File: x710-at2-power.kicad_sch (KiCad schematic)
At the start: 6 parts, among them U1 EZX710AT2_S_LMR5

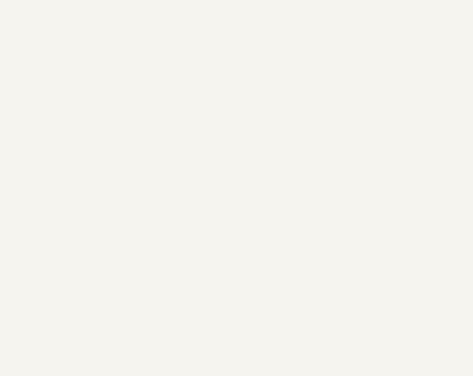
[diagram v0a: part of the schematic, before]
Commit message: [#80813] Add RJ45 connectors, add SMBus, FLASH SPI and misc
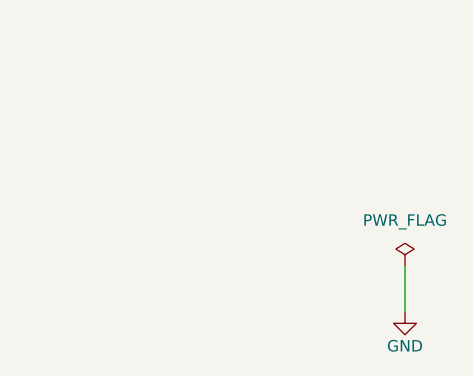
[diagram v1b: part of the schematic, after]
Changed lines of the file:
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@@
+	(wire
+		(pts
+			(xy 331.47 175.26) (xy 331.47 180.34)
+		)
+		(stroke
+			(width 0)
+			(type default)
+		)
+	)
 	(wire
 		(pts
@@
 					(unit 1)
 				)
+			)
+		)
+	)
+	(symbol
+		(lib_id "antmicropower:PWR_FLAG")
+		(at 331.47 175.26 0)
+		(unit 1)
+		(exclude_from_sim no)
+		(in_bom yes)
+		(on_board yes)
+		(dnp no)
+		(fields_autoplaced yes)
+		(property "Reference" "#FLG01"
+			(at 331.47 173.355 0)
+			(effects
+				(font
+					(size 1.27 1.27)
+				)
+				(hide yes)
+			)
+		)
+		(property "Value" "PWR_FLAG"
+			(at 331.47 170.18 0)
+			(effects
+				(font
+					(size 1.27 1.27)
+				)
+			)
+		)
+		(property "Footprint" ""
+			(at 331.47 175.26 0)
+			(effects
+				(font
+					(size 1.27 1.27)
+				)
+				(hide yes)
+			)
+		)
+		(property "Datasheet" ""
+			(at 331.47 175.26 0)
+			(effects
+				(font
+					(size 1.27 1.27)
+				)
+				(hide yes)
+			)
+		)
+		(property "Description" ""
+			(at 331.47 175.26 0)
+			(effects
+				(font
+					(size 1.27 1.27)
+				)
+				(hide yes)
+			)
+		)
+		(pin "1"
+		)
+		(instances
+			(project ""
+				(path "/04bda987-e5eb-48b4-9e90-d8211dc11b39/745fdd8b-25af-4553-a7ea-a0fa564ee0a7"
+					(reference "#FLG01")
+					(unit 1)
+				)
+			)
+		)
+	)
+	(symbol
+		(lib_id "antmicropower:GND")
+		(at 331.47 180.34 0)
+		(unit 1)
+		(exclude_from_sim no)
+		(in_bom yes)
+		(on_board yes)
+		(dnp no)
+		(property "Reference" "#PWR053"
+			(at 340.36 182.88 0)
+			(effects
+				(font
+					(size 1.27 1.27)
+					(thickness 0.15)
+				)
+				(justify left bottom)
+				(hide yes)
+			)
+		)
+		(property "Value" "GND"
+			(at 331.47 184.15 0)
+			(effects
+				(font
+					(size 1.27 1.27)
+					(thickness 0.15)
+				)
+			)
+		)
+		(property "Footprint" ""
+			(at 340.36 187.96 0)
+			(effects
+				(font
+					(size 1.27 1.27)
+					(thickness 0.15)
+				)
+				(justify left bottom)
+				(hide yes)
+			)
+		)
+		(property "Datasheet" ""
+			(at 340.36 193.04 0)
+			(effects
+				(font
+					(size 1.27 1.27)
+					(thickness 0.15)
+				)
+				(justify left bottom)
+				(hide yes)
+			)
+		)
+		(property "Description" ""
+			(at 331.47 180.34 0)
+			(effects
+				(font
+					(size 1.27 1.27)
+				)
+				(hide yes)
+			)
+		)
+		(property "Author" "Antmicro"
+			(at 340.36 187.96 0)
+			(effects
+				(font
+					(size 1.27 1.27)
+					(thickness 0.15)
+				)
+				(justify left bottom)
+				(hide yes)
+			)
+		)
+		(property "License" "Apache-2.0"
+			(at 340.36 190.5 0)
+			(effects
+				(font
+					(size 1.27 1.27)
+					(thickness 0.15)
+				)
+				(justify left bottom)
+				(hide yes)
+			)
+		)
+		(pin "1"
+		)
+		(instances
+			(project "10-gbe-expansion"
+				(path "/04bda987-e5eb-48b4-9e90-d8211dc11b39/745fdd8b-25af-4553-a7ea-a0fa564ee0a7"
+					(reference "#PWR053")
+					(unit 1)
+				)

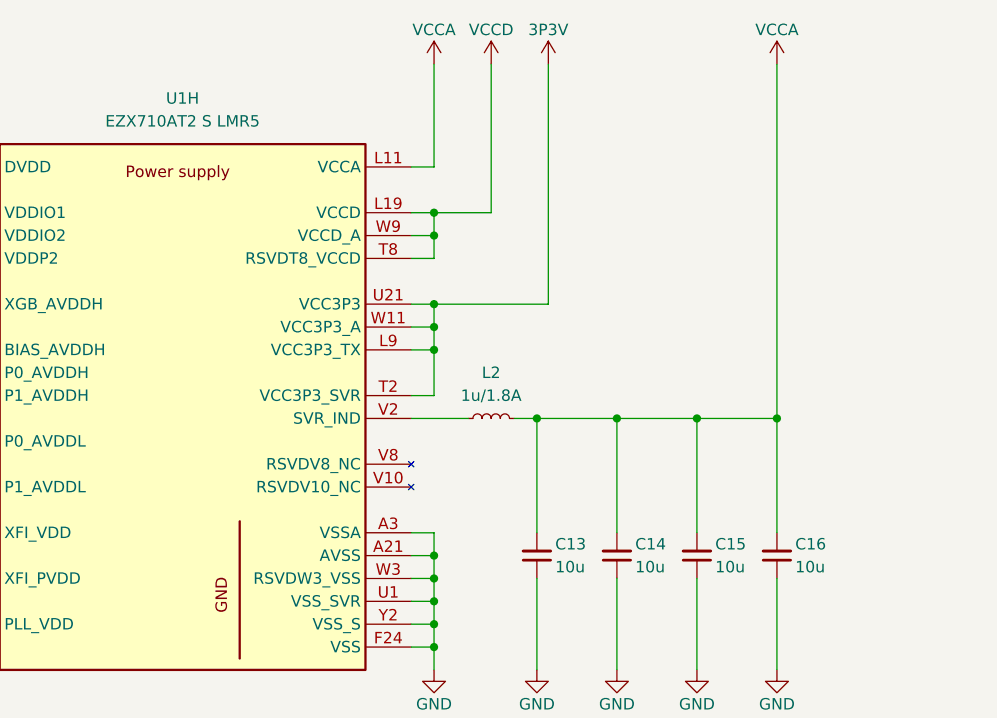
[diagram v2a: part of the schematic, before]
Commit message: [#80813] Change RJ45 connectors, reannotate schematics
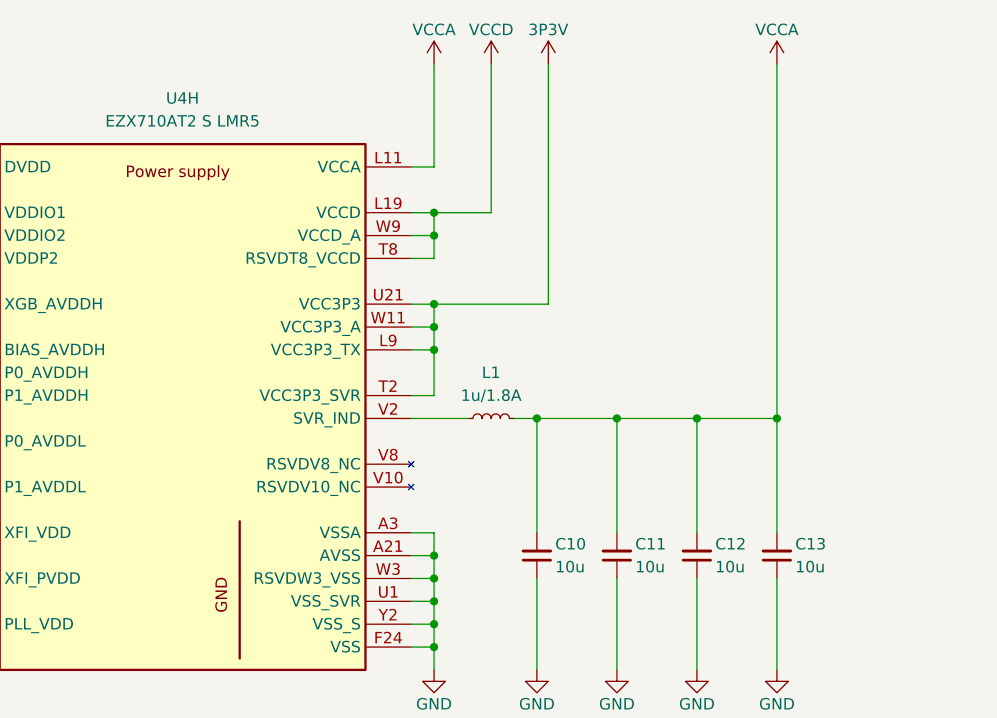
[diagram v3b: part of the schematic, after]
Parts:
- renumbered C13 to C10, C14 to C11, C15 to C12, C16 to C13, L2 to L1, U1 to U4
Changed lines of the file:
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@@
 		(on_board yes)
 		(dnp no)
-		(property "Reference" "C13"
+		(property "Reference" "C10"
 			(at 253.492 166.37 90)
 			(effects
@@
 			(project "10-gbe-expansion"
 				(path "/04bda987-e5eb-48b4-9e90-d8211dc11b39/745fdd8b-25af-4553-a7ea-a0fa564ee0a7"
-					(reference "C13")
+					(reference "C10")
 					(unit 1)
 				)
@@
 		(on_board yes)
 		(dnp no)
-		(property "Reference" "C16"
+		(property "Reference" "C13"
 			(at 280.162 166.37 90)
 			(effects
@@
 			(project "10-gbe-expansion"
 				(path "/04bda987-e5eb-48b4-9e90-d8211dc11b39/745fdd8b-25af-4553-a7ea-a0fa564ee0a7"
-					(reference "C16")
+					(reference "C13")
 					(unit 1)
 				)
@@
 		(on_board yes)
 		(dnp no)
-		(property "Reference" "#PWR035"
+		(property "Reference" "#PWR039"
 			(at 278.13 116.84 0)
 			(effects
@@
 			(project "10-gbe-expansion"
 				(path "/04bda987-e5eb-48b4-9e90-d8211dc11b39/745fdd8b-25af-4553-a7ea-a0fa564ee0a7"
-					(reference "#PWR035")
+					(reference "#PWR039")
 					(unit 1)
 				)
@@
 		(on_board yes)
 		(dnp no)
-		(property "Reference" "#PWR031"
+		(property "Reference" "#PWR041"
 			(at 260.35 182.88 0)
 			(effects
@@
 			(project "10-gbe-expansion"
 				(path "/04bda987-e5eb-48b4-9e90-d8211dc11b39/745fdd8b-25af-4553-a7ea-a0fa564ee0a7"
-					(reference "#PWR031")
+					(reference "#PWR041")
 					(unit 1)
 				)
@@
 		(on_board yes)
 		(dnp no)
-		(property "Reference" "#PWR033"
+		(property "Reference" "#PWR042"
 			(at 269.24 182.88 0)
 			(effects
@@
 			(project "10-gbe-expansion"
 				(path "/04bda987-e5eb-48b4-9e90-d8211dc11b39/745fdd8b-25af-4553-a7ea-a0fa564ee0a7"
-					(reference "#PWR033")
+					(reference "#PWR042")
 					(unit 1)
 				)
@@
 		(on_board yes)
 		(dnp no)
-		(property "Reference" "#PWR053"
+		(property "Reference" "#PWR045"
 			(at 340.36 182.88 0)
 			(effects
@@
 			(project "10-gbe-expansion"
 				(path "/04bda987-e5eb-48b4-9e90-d8211dc11b39/745fdd8b-25af-4553-a7ea-a0fa564ee0a7"
-					(reference "#PWR053")
+					(reference "#PWR045")
 					(unit 1)
 				)
@@
 		(on_board yes)
 		(dnp no)
-		(property "Reference" "C15"
+		(property "Reference" "C12"
 			(at 271.272 166.37 90)
 			(effects
@@
 			(project "10-gbe-expansion"
 				(path "/04bda987-e5eb-48b4-9e90-d8211dc11b39/745fdd8b-25af-4553-a7ea-a0fa564ee0a7"
-					(reference "C15")
+					(reference "C12")
 					(unit 1)
 				)
@@
 		(on_board yes)
 		(dnp no)
-		(property "Reference" "#PWR025"
+		(property "Reference" "#PWR033"
 			(at 166.37 116.84 0)
 			(effects
@@
 			(project "10-gbe-expansion"
 				(path "/04bda987-e5eb-48b4-9e90-d8211dc11b39/745fdd8b-25af-4553-a7ea-a0fa564ee0a7"
-					(reference "#PWR025")
+					(reference "#PWR033")
 					(unit 1)
 				)
@@
 		(on_board yes)
 		(dnp no)
-		(property "Reference" "#PWR027"
+		(property "Reference" "#PWR035"
 			(at 184.15 116.84 0)
 			(effects
@@
 			(project "10-gbe-expansion"
 				(path "/04bda987-e5eb-48b4-9e90-d8211dc11b39/745fdd8b-25af-4553-a7ea-a0fa564ee0a7"
-					(reference "#PWR027")
+					(reference "#PWR035")
 					(unit 1)
 				)
@@
 		(dnp no)
 		(fields_autoplaced yes)
-		(property "Reference" "L2"
+		(property "Reference" "L1"
 			(at 246.38 147.32 0)
 			(effects
@@
 			(project "10-gbe-expansion"
 				(path "/04bda987-e5eb-48b4-9e90-d8211dc11b39/745fdd8b-25af-4553-a7ea-a0fa564ee0a7"
-					(reference "L2")
+					(reference "L1")
 					(unit 1)
 				)
@@
 		(on_board yes)
 		(dnp no)
-		(property "Reference" "#PWR020"
+		(property "Reference" "#PWR028"
 			(at 114.3 116.84 0)
 			(effects
@@
 			(project "10-gbe-expansion"
 				(path "/04bda987-e5eb-48b4-9e90-d8211dc11b39/745fdd8b-25af-4553-a7ea-a0fa564ee0a7"
-					(reference "#PWR020")
+					(reference "#PWR028")
 					(unit 1)
 				)
@@
 		(dnp no)
 		(fields_autoplaced yes)
-		(property "Reference" "U1"
+		(property "Reference" "U4"
 			(at 212.09 116.84 0)
 			(effects
@@
 			(project "10-gbe-expansion"
 				(path "/04bda987-e5eb-48b4-9e90-d8211dc11b39/745fdd8b-25af-4553-a7ea-a0fa564ee0a7"
-					(reference "U1")
+					(reference "U4")
 					(unit 8)
 				)
@@
 		(on_board yes)
 		(dnp no)
-		(property "Reference" "#PWR036"
+		(property "Reference" "#PWR044"
 			(at 287.02 182.88 0)
 			(effects
@@
 			(project "10-gbe-expansion"
 				(path "/04bda987-e5eb-48b4-9e90-d8211dc11b39/745fdd8b-25af-4553-a7ea-a0fa564ee0a7"
-					(reference "#PWR036")
+					(reference "#PWR044")
 					(unit 1)
 				)
@@
 		(on_board yes)
 		(dnp no)
-		(property "Reference" "C14"
+		(property "Reference" "C11"
 			(at 262.382 166.37 90)
 			(effects
@@
 			(project "10-gbe-expansion"
 				(path "/04bda987-e5eb-48b4-9e90-d8211dc11b39/745fdd8b-25af-4553-a7ea-a0fa564ee0a7"
-					(reference "C14")
+					(reference "C11")
 					(unit 1)
 				)
@@
 		(on_board yes)
 		(dnp no)
-		(property "Reference" "#PWR024"
+		(property "Reference" "#PWR032"
 			(at 156.21 116.84 0)
 			(effects
@@
 			(project "10-gbe-expansion"
 				(path "/04bda987-e5eb-48b4-9e90-d8211dc11b39/745fdd8b-25af-4553-a7ea-a0fa564ee0a7"
-					(reference "#PWR024")
+					(reference "#PWR032")
 					(unit 1)
 				)
@@
 		(on_board yes)
 		(dnp no)
-		(property "Reference" "#PWR034"
+		(property "Reference" "#PWR043"
 			(at 278.13 182.88 0)
 			(effects
@@
 			(project "10-gbe-expansion"
 				(path "/04bda987-e5eb-48b4-9e90-d8211dc11b39/745fdd8b-25af-4553-a7ea-a0fa564ee0a7"
-					(reference "#PWR034")
+					(reference "#PWR043")
 					(unit 1)
 				)
@@
 		(on_board yes)
 		(dnp no)
-		(property "Reference" "#PWR021"
+		(property "Reference" "#PWR029"
 			(at 124.46 116.84 0)
 			(effects
@@
 			(project "10-gbe-expansion"
 				(path "/04bda987-e5eb-48b4-9e90-d8211dc11b39/745fdd8b-25af-4553-a7ea-a0fa564ee0a7"
-					(reference "#PWR021")
+					(reference "#PWR029")
 					(unit 1)
 				)
@@
 		(on_board yes)
 		(dnp no)
-		(property "Reference" "#PWR029"
+		(property "Reference" "#PWR040"
 			(at 248.92 182.88 0)
 			(effects
@@
 			(project "10-gbe-expansion"
 				(path "/04bda987-e5eb-48b4-9e90-d8211dc11b39/745fdd8b-25af-4553-a7ea-a0fa564ee0a7"
-					(reference "#PWR029")
+					(reference "#PWR040")
 					(unit 1)
 				)
@@
 		(on_board yes)
 		(dnp no)
-		(property "Reference" "#PWR030"
+		(property "Reference" "#PWR037"
 			(at 246.38 116.84 0)
 			(effects
@@
 			(project "10-gbe-expansion"
 				(path "/04bda987-e5eb-48b4-9e90-d8211dc11b39/745fdd8b-25af-4553-a7ea-a0fa564ee0a7"
-					(reference "#PWR030")
+					(reference "#PWR037")
 					(unit 1)
 				)
@@
 		(on_board yes)
 		(dnp no)
-		(property "Reference" "#PWR019"
+		(property "Reference" "#PWR027"
 			(at 104.14 116.84 0)
 			(effects
@@
 			(project "10-gbe-expansion"
 				(path "/04bda987-e5eb-48b4-9e90-d8211dc11b39/745fdd8b-25af-4553-a7ea-a0fa564ee0a7"
-					(reference "#PWR019")
+					(reference "#PWR027")
 					(unit 1)
 				)
@@
 		(on_board yes)
 		(dnp no)
-		(property "Reference" "#PWR032"
+		(property "Reference" "#PWR038"
 			(at 252.73 116.84 0)
 			(effects
@@
 			(project "10-gbe-expansion"
 				(path "/04bda987-e5eb-48b4-9e90-d8211dc11b39/745fdd8b-25af-4553-a7ea-a0fa564ee0a7"
-					(reference "#PWR032")
+					(reference "#PWR038")
 					(unit 1)
 				)
@@
 		(on_board yes)
 		(dnp no)
-		(property "Reference" "#PWR022"
+		(property "Reference" "#PWR030"
 			(at 134.62 116.84 0)
 			(effects
@@
 			(project "10-gbe-expansion"
 				(path "/04bda987-e5eb-48b4-9e90-d8211dc11b39/745fdd8b-25af-4553-a7ea-a0fa564ee0a7"
-					(reference "#PWR022")
+					(reference "#PWR030")
 					(unit 1)
 				)
@@
 		(on_board yes)
 		(dnp no)
-		(property "Reference" "#PWR026"
+		(property "Reference" "#PWR034"
 			(at 176.53 116.84 0)
 			(effects
@@
 			(project "10-gbe-expansion"
 				(path "/04bda987-e5eb-48b4-9e90-d8211dc11b39/745fdd8b-25af-4553-a7ea-a0fa564ee0a7"
-					(reference "#PWR026")
+					(reference "#PWR034")
 					(unit 1)
 				)
@@
 		(on_board yes)
 		(dnp no)
-		(property "Reference" "#PWR023"
+		(property "Reference" "#PWR031"
 			(at 146.05 116.84 0)
 			(effects
@@
 			(project "10-gbe-expansion"
 				(path "/04bda987-e5eb-48b4-9e90-d8211dc11b39/745fdd8b-25af-4553-a7ea-a0fa564ee0a7"
-					(reference "#PWR023")
+					(reference "#PWR031")
 					(unit 1)
 				)
@@
 		(on_board yes)
 		(dnp no)
-		(property "Reference" "#PWR028"
+		(property "Reference" "#PWR036"
 			(at 240.03 116.84 0)
 			(effects
@@
 			(project "10-gbe-expansion"
 				(path "/04bda987-e5eb-48b4-9e90-d8211dc11b39/745fdd8b-25af-4553-a7ea-a0fa564ee0a7"
-					(reference "#PWR028")
+					(reference "#PWR036")
 					(unit 1)
 				)

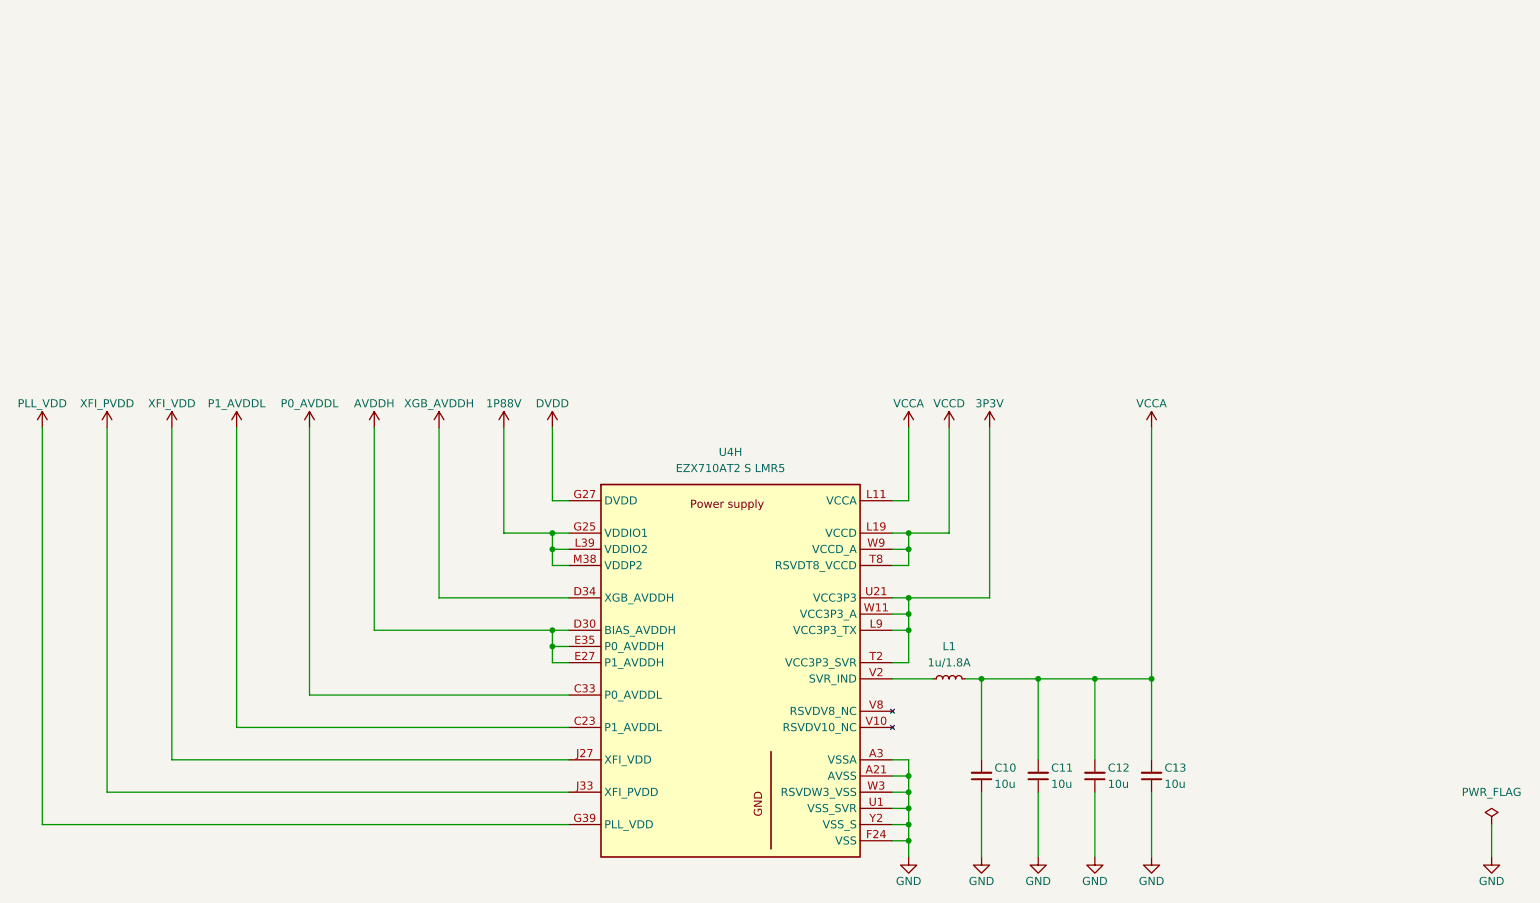
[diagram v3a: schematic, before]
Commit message: [#80813] Improve schematic readability, add debug connectors and missing resistors
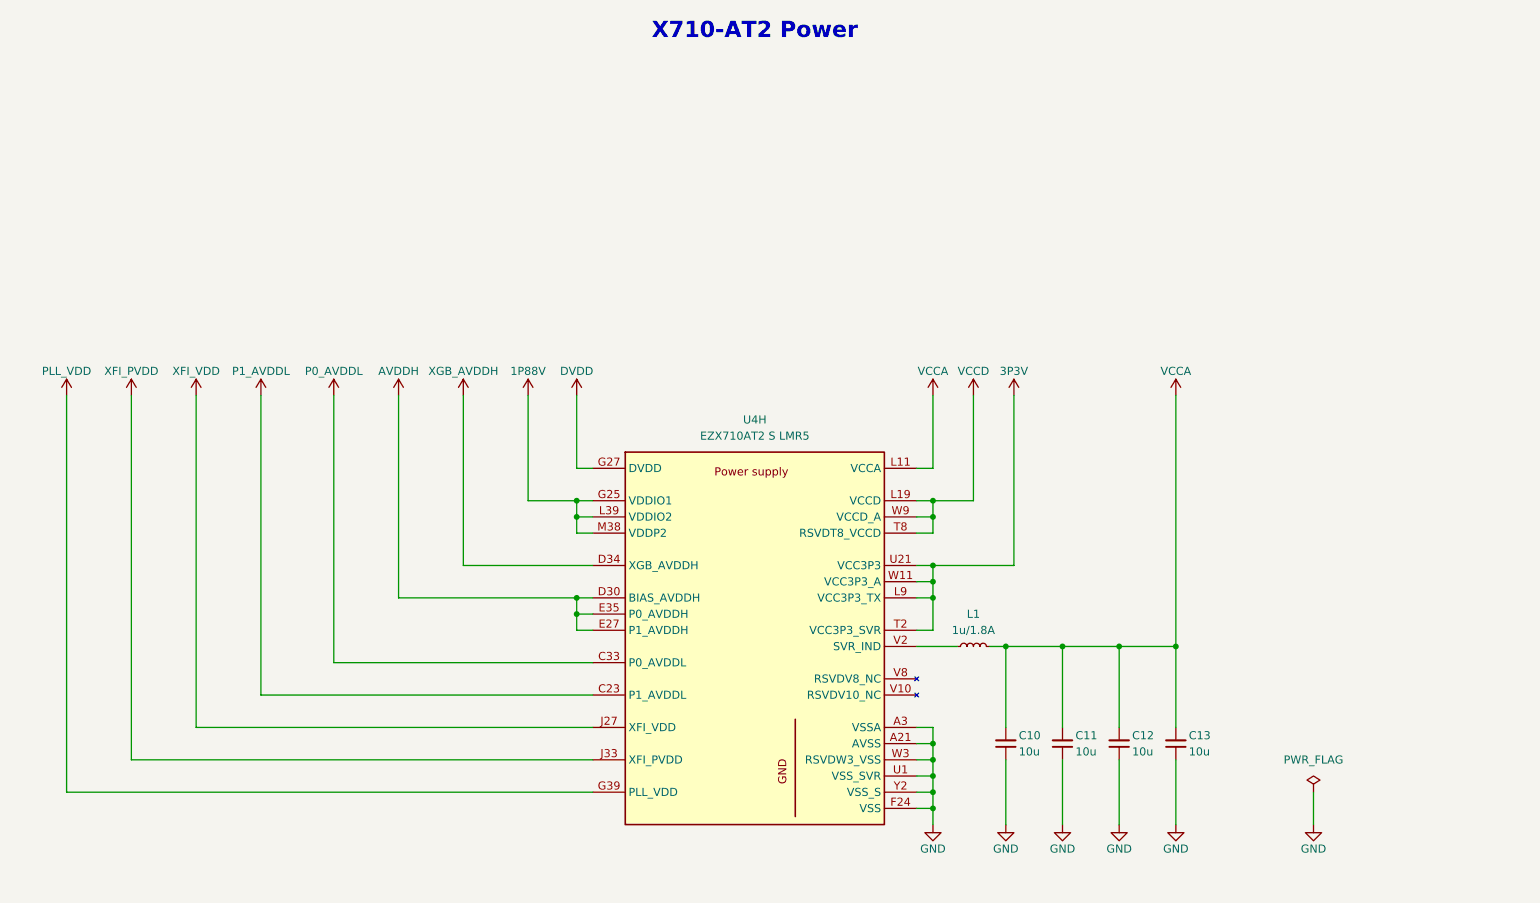
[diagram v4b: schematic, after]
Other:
- note added: "X710-AT2 Power"
- moved on the sheet: C10, C11, C12, C13, L1, U4H
